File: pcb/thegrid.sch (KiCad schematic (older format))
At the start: 47 parts, among them P1 CONN_2, P10 CONN_2, P2 CONN_2, P3 POWER, P4 CONN_2, P5 CONN_2, P6 SHIFT_IN, P7 CONN_2, P8 SHIFT_OUT, P9 CONN_2, Q1 FQP7P06, Q2 FQP7P06, Q3 FQP7P06, Q4 FQP7P06, Q5 FQP7P06, Q6 FQP7P06, Q7 FQP7P06, U1 7805, U2 TPIC6C595

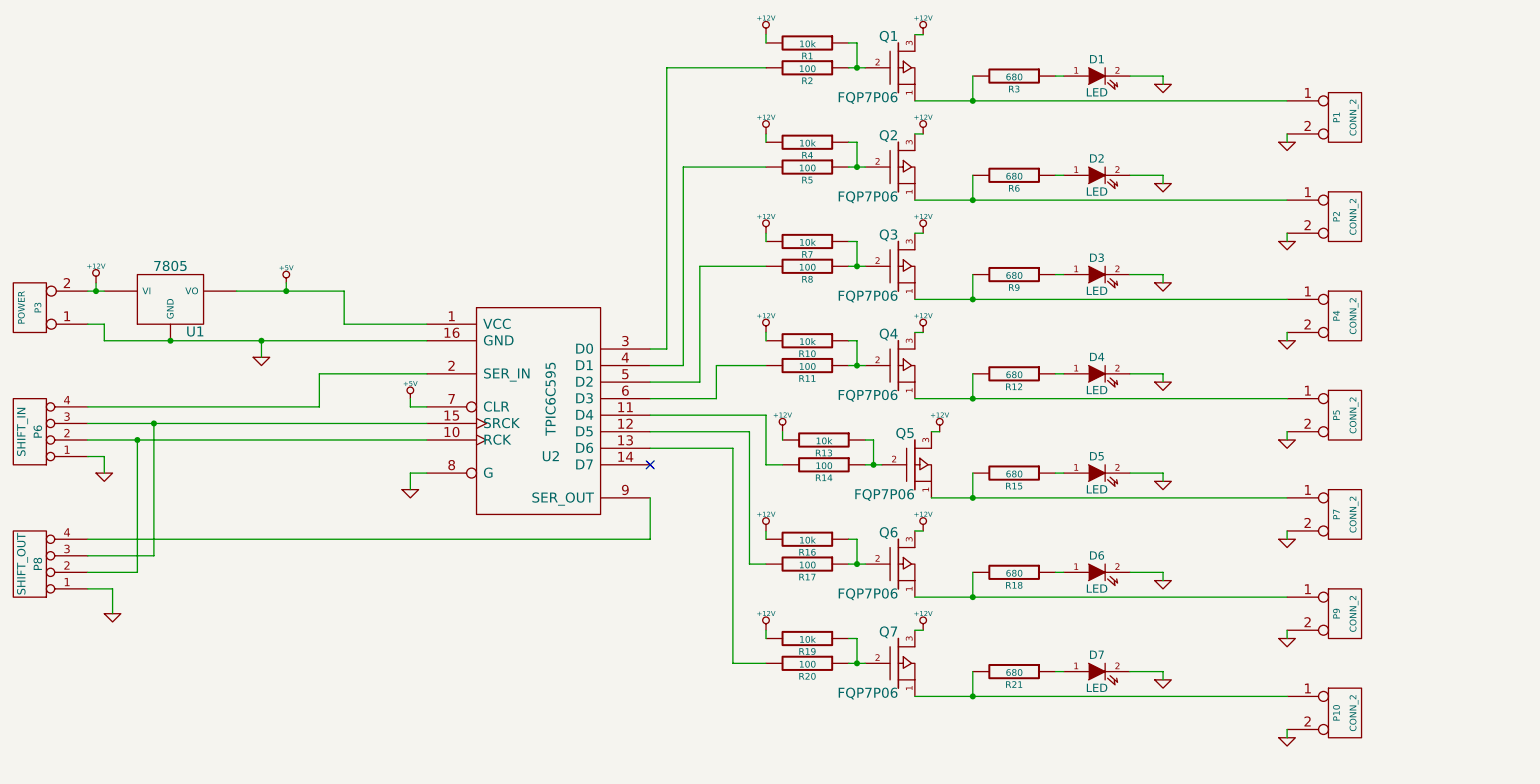
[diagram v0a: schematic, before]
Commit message: Schematic touchups and PCB footprint layout
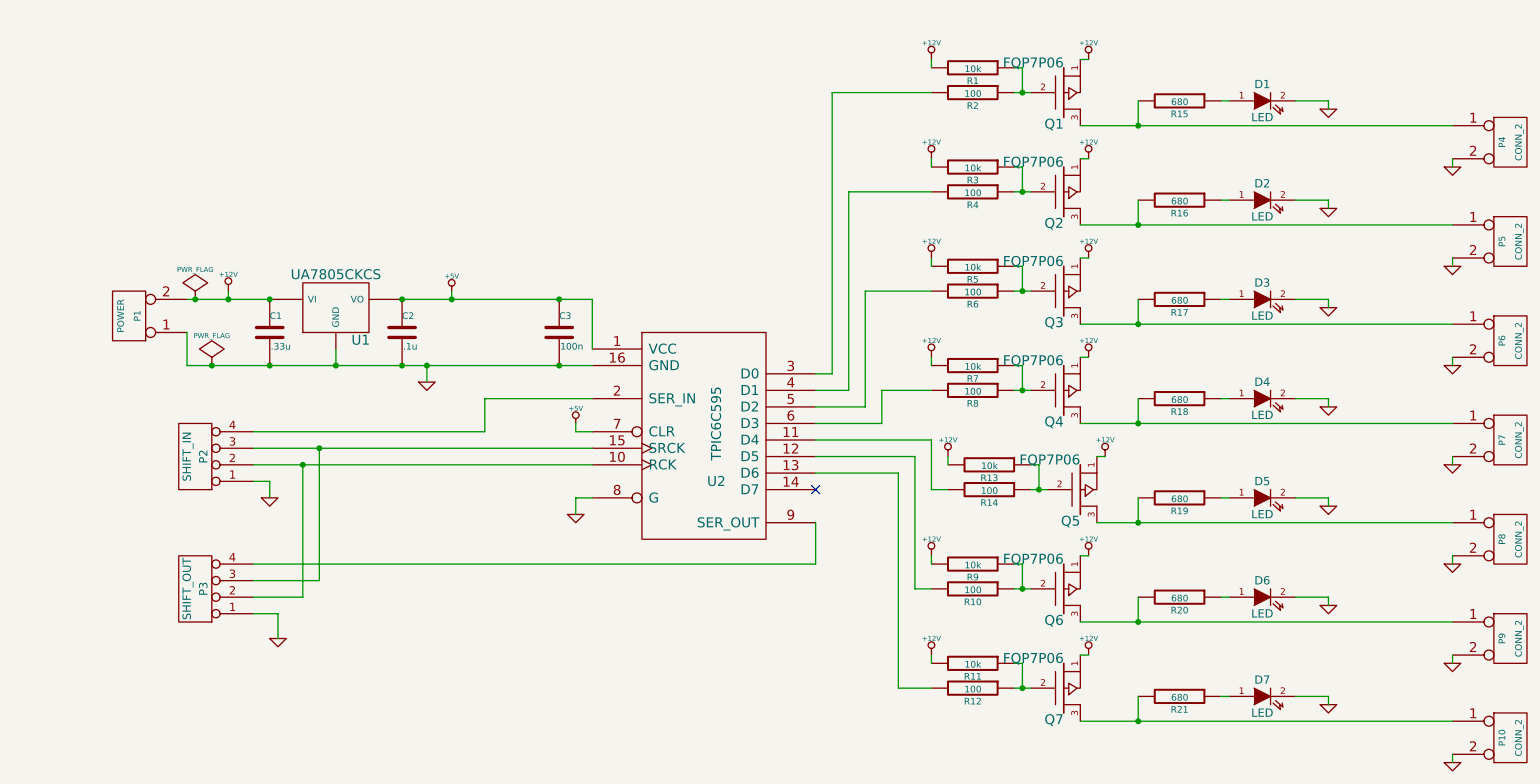
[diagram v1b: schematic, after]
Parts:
- added C1: .33u, symbol C
- added C2: .1u, symbol C
- added C3: 100n, symbol C
- U1: value 7805 -> UA7805CKCS
- renumbered P3 to P1, P6 to P2, P8 to P3, P1 to P4, P2 to P5, P4 to P6, P5 to P7, P7 to P8, R17 to R10, R19 to R11, R20 to R12, R3 to R15, R6 to R16, R9 to R17, R12 to R18, R15 to R19, R18 to R20, R4 to R3, R5 to R4, R7 to R5, R8 to R6, R10 to R7, R11 to R8, R16 to R9
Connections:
- net +12V: now also Q1.1 (S), Q2.1 (S), Q3.1 (S), Q4.1 (S), Q5.1 (S), Q6.1 (S), Q7.1 (S), C1.1; no longer Q1.3 (D), Q2.3 (D), Q3.3 (D), Q4.3 (D), Q5.3 (D), Q6.3 (D), Q7.3 (D)
- net +5V: now also C2.1, C3.1
- net GND: now also C1.2, C2.2, C3.2
- net at P4.1 (P1), R15.2: now also Q1.3 (D); no longer Q1.1 (S)
- net at P5.1 (P1), R16.2: now also Q2.3 (D); no longer Q2.1 (S)
- net at P6.1 (P1), R17.2: now also Q3.3 (D); no longer Q3.1 (S)
- net at P7.1 (P1), R18.2: now also Q4.3 (D); no longer Q4.1 (S)
- net at P8.1 (P1), R19.2: now also Q5.3 (D); no longer Q5.1 (S)
- net at P9.1 (P1), R20.2: now also Q6.3 (D); no longer Q6.1 (S)
- net at P10.1 (P1), R21.2: now also Q7.3 (D); no longer Q7.1 (S)
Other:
- moved on the sheet: D1, D2, D3, D4, D5, D6, D7, P1, P10, P2, P3, P4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

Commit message: cosmetic changes to schematic
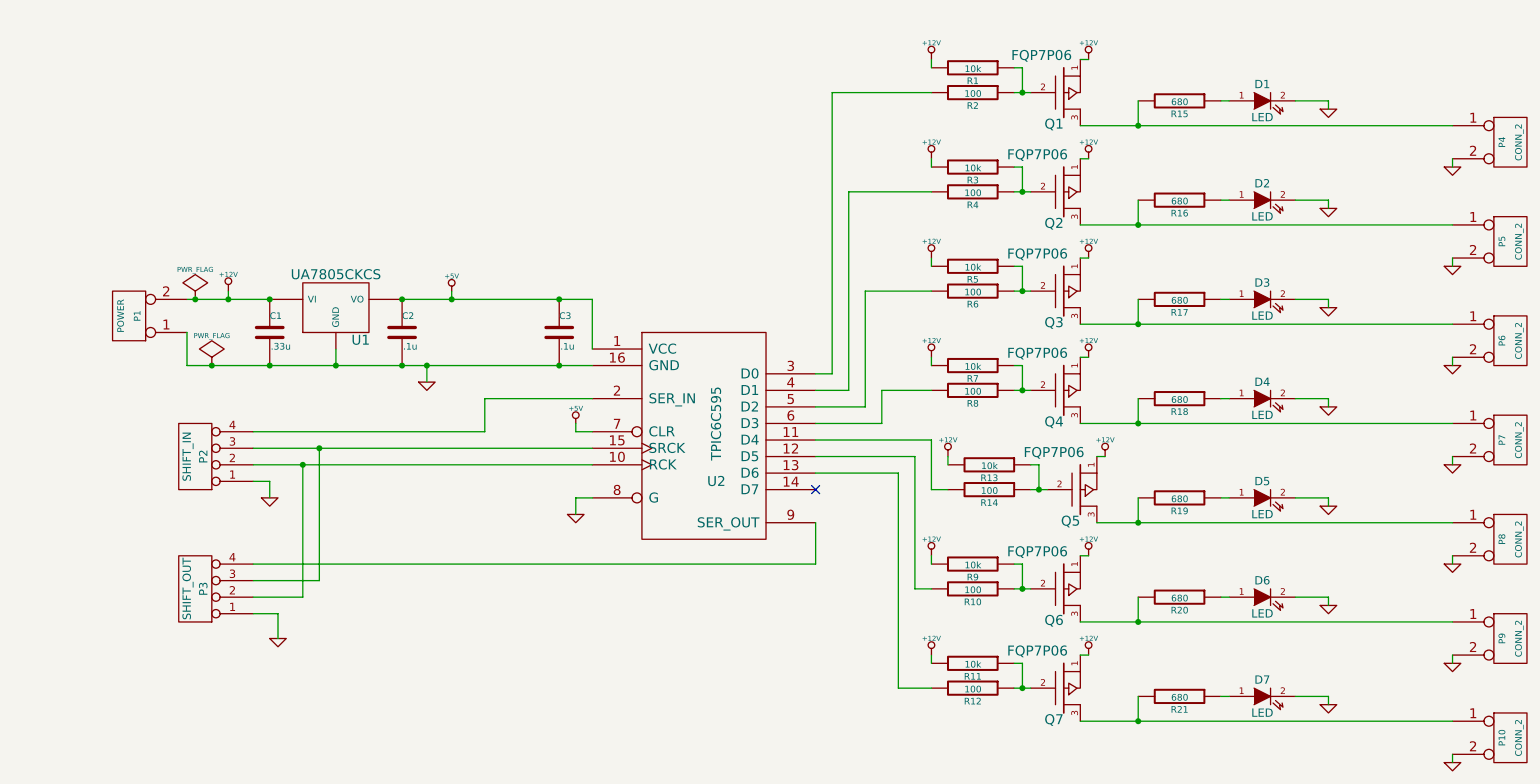
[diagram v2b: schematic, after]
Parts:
- C3: value 100n -> .1u
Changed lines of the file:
@@
 P 6900 1550
 F 0 "Q1" H 6900 1740 60  0000 R CNN
-F 1 "FQP7P06" H 6900 1370 60  0000 R CNN
+F 1 "FQP7P06" H 6950 1325 60  0000 R CNN
 F 2 "" H 6900 1550 60  0000 C CNN
 F 3 "" H 6900 1550 60  0000 C CNN
@@
 P 6900 2150
 F 0 "Q2" H 6900 2340 60  0000 R CNN
-F 1 "FQP7P06" H 6900 1970 60  0000 R CNN
+F 1 "FQP7P06" H 6925 1925 60  0000 R CNN
 F 2 "" H 6900 2150 60  0000 C CNN
 F 3 "" H 6900 2150 60  0000 C CNN
@@
 P 6900 2750
 F 0 "Q3" H 6900 2940 60  0000 R CNN
-F 1 "FQP7P06" H 6900 2570 60  0000 R CNN
+F 1 "FQP7P06" H 6925 2525 60  0000 R CNN
 F 2 "" H 6900 2750 60  0000 C CNN
 F 3 "" H 6900 2750 60  0000 C CNN
@@
 P 6900 3350
 F 0 "Q4" H 6900 3540 60  0000 R CNN
-F 1 "FQP7P06" H 6900 3170 60  0000 R CNN
+F 1 "FQP7P06" H 6925 3125 60  0000 R CNN
 F 2 "" H 6900 3350 60  0000 C CNN
 F 3 "" H 6900 3350 60  0000 C CNN
@@
 P 7000 3950
 F 0 "Q5" H 7000 4140 60  0000 R CNN
-F 1 "FQP7P06" H 7000 3770 60  0000 R CNN
+F 1 "FQP7P06" H 7025 3725 60  0000 R CNN
 F 2 "" H 7000 3950 60  0000 C CNN
 F 3 "" H 7000 3950 60  0000 C CNN
@@
 P 6900 4550
 F 0 "Q6" H 6900 4740 60  0000 R CNN
-F 1 "FQP7P06" H 6900 4370 60  0000 R CNN
+F 1 "FQP7P06" H 6925 4325 60  0000 R CNN
 F 2 "" H 6900 4550 60  0000 C CNN
 F 3 "" H 6900 4550 60  0000 C CNN
@@
 P 6900 5150
 F 0 "Q7" H 6900 5340 60  0000 R CNN
-F 1 "FQP7P06" H 6900 4970 60  0000 R CNN
+F 1 "FQP7P06" H 6925 4925 60  0000 R CNN
 F 2 "" H 6900 5150 60  0000 C CNN
 F 3 "" H 6900 5150 60  0000 C CNN
@@
 P 3850 3000
 F 0 "C3" H 3850 3100 40  0000 L CNN
-F 1 "100n" H 3856 2915 40  0000 L CNN
+F 1 ".1u" H 3856 2915 40  0000 L CNN
 F 2 "" H 3888 2850 30  0000 C CNN
 F 3 "" H 3850 3000 60  0000 C CNN
